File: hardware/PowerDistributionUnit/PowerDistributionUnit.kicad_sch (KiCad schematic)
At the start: 28 parts, among them J0 Conn_01x02, J1 Conn_01x02, J10 Conn_01x02, J11 Conn_01x02, J12 Conn_01x02, J13 Conn_01x02, J14 Conn_01x04, J15 Conn_01x04, J16 Conn_01x02, J2 Conn_01x02, J3 Conn_01x02, J4 Conn_01x02, J5 Conn_01x02, J6 Conn_01x02, J7 Conn_01x02, J8 Conn_01x02, J9 Conn_01x02

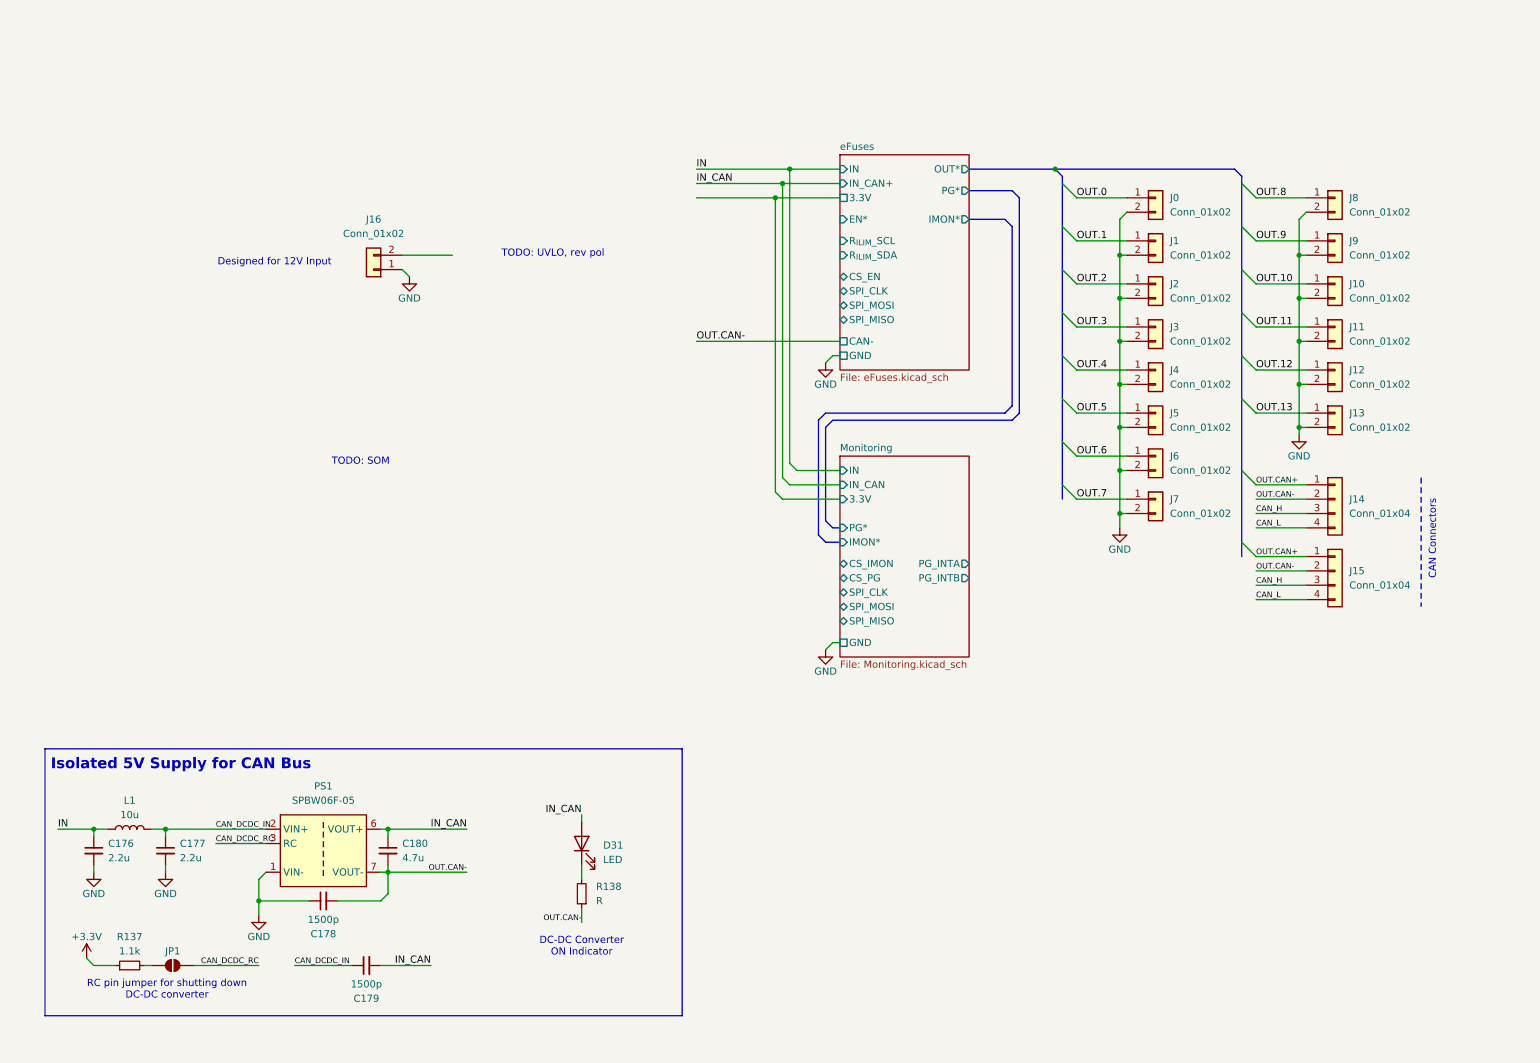
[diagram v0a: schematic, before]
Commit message: Added PSOM
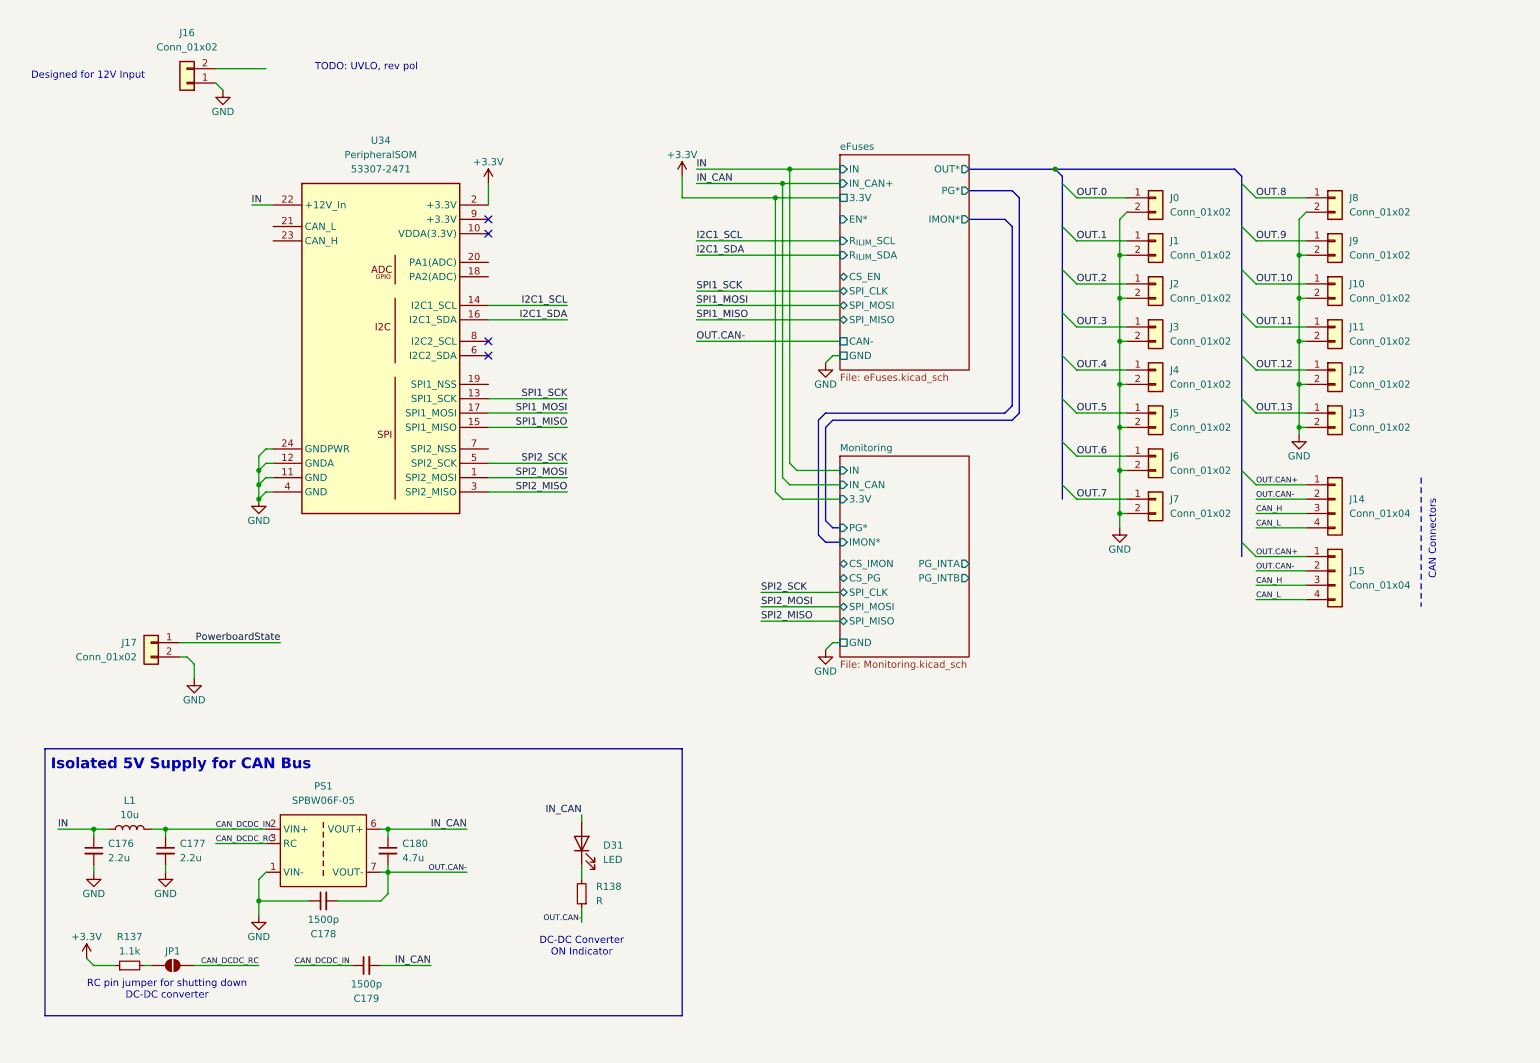
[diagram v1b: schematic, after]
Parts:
- added J17: Conn_01x02, symbol Connector_Generic:Conn_01x02
- added U34: PeripheralSOM, UTSVT_Special:PeripheralSOM, symbol utsvt-misc:PeripheralSOM
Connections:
- net +3.3V: now also U34.2 (+3.3V)
- net GND: now also J17.2 (Pin_2), U34.11 (GND), U34.12 (GNDA), U34.24 (GNDPWR), U34.4 (GND)
- net IN: now also U34.22 (+12V_In)
- new net I2C1_SCL: U34.14 (I2C1_SCL)
- new net I2C1_SDA: U34.16 (I2C1_SDA)
- new net PowerboardState: J17.1 (Pin_1)
- new net SPI1_MISO: U34.15 (SPI1_MISO)
- new net SPI1_MOSI: U34.17 (SPI1_MOSI)
- new net SPI1_SCK: U34.13 (SPI1_SCK)
- new net SPI2_MISO: U34.3 (SPI2_MISO)
- new net SPI2_MOSI: U34.1 (SPI2_MOSI)
- new net SPI2_SCK: U34.5 (SPI2_SCK)
- no-connect marks 0 -> 4
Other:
- note removed: "TODO: SOM"
- moved on the sheet: J16

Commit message: Added footprints, added pull-up resistors, finished wiring up SOM
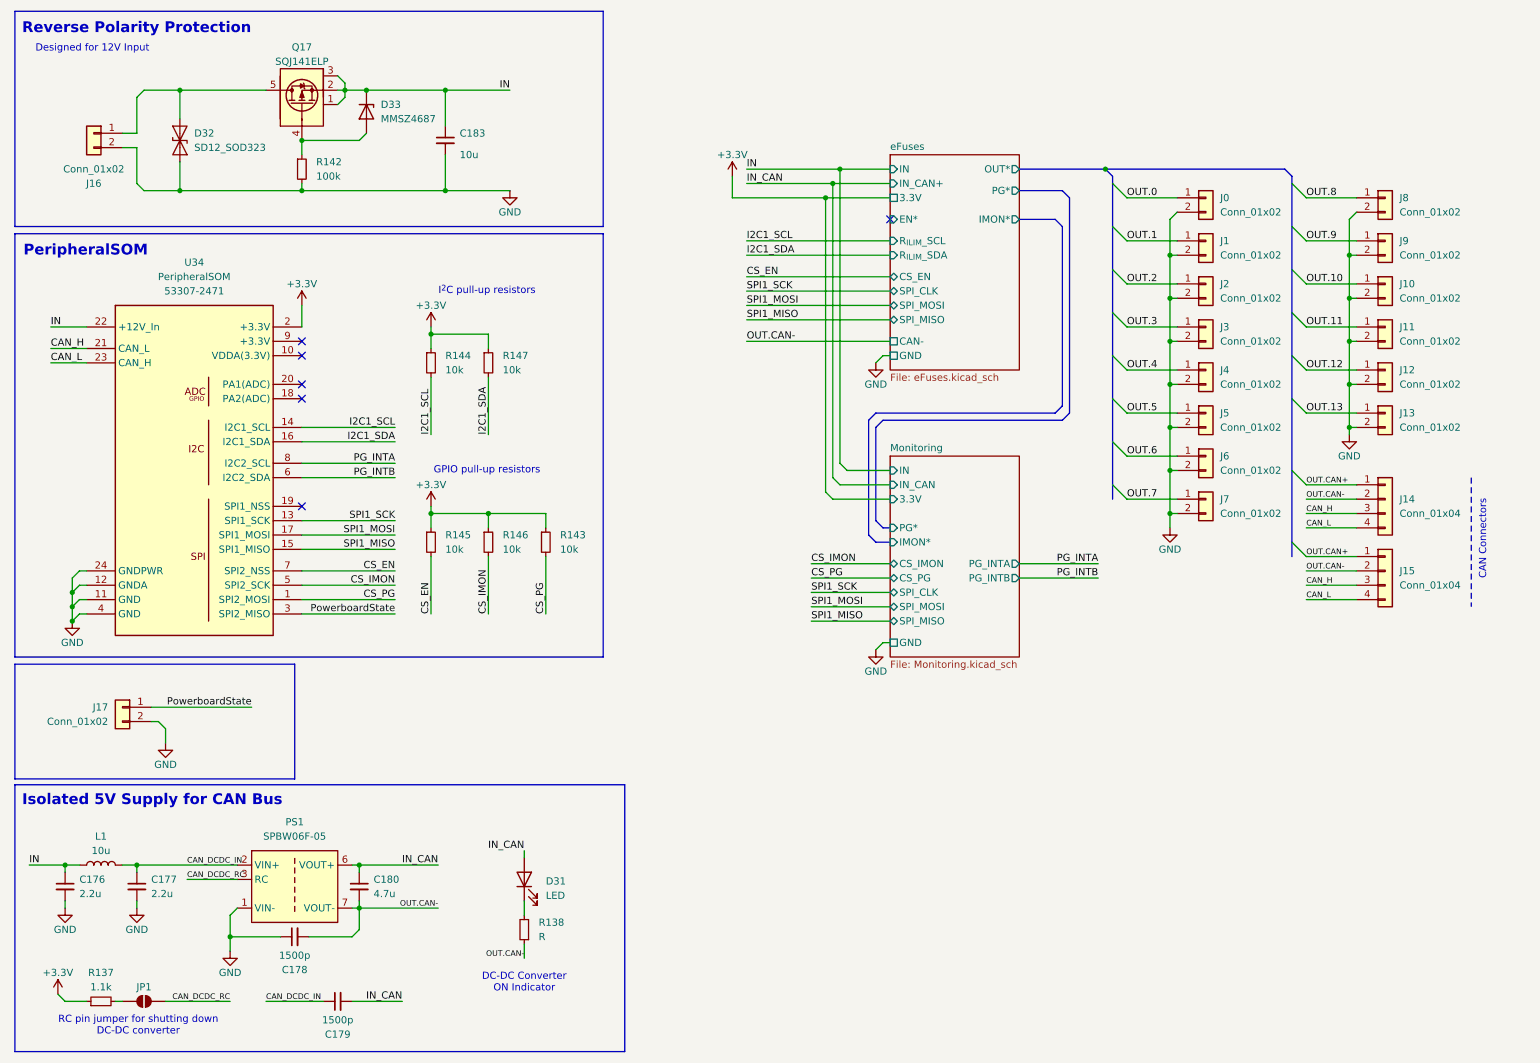
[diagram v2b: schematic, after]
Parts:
- added C183: 10u, symbol Device:C_Small
- added D32: SD12_SOD323, Diode_SMD:D_SOD-323, symbol Diode:SD12_SOD323
- added D33: MMSZ4687, Diode_SMD:D_SOD-123, symbol Device:D_Zener
- added Q17: SQJ141ELP, Package_SO:PowerPAK_SO-8L_Single, symbol PowerDistributionUnitLib:SQJ141ELP
- added R142: 100k, symbol Device:R_Small
- added R143, R144, R145, R146, R147: 10k, symbol Device:R_Small
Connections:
- net SPI2_MISO is gone; now on net PowerboardState: U34.3 (SPI2_MISO)
- net +3.3V: now also R143.1, R144.1, R145.1, R146.1, R147.1
- net CAN_H: now also U34.21 (CAN_L)
- net CAN_L: now also U34.23 (CAN_H)
- net GND: now also J16.2 (Pin_2), C183.2, D32.1 (A1), R142.2; no longer J16.1 (Pin_1)
- net I2C1_SCL: now also R144.2
- net I2C1_SDA: now also R147.2
- net IN: now also C183.1, D33.1 (K), Q17.1, Q17.2, Q17.3
- net PG_INTB: now reaches U34.6 (I2C2_SDA)
- net CS_EN: now reaches U34.7 (SPI2_NSS)
- net CS_EN: now also R145.2
- net PG_INTA: now reaches U34.8 (I2C2_SCL)
- net SPI2_MOSI renamed CS_PG
- net CS_PG: now also R143.2
- net SPI2_SCK renamed CS_IMON
- net CS_IMON: now also R146.2
- new net: D32.2 (A2), J16.1 (Pin_1), Q17.5
- new net: D33.2 (A), Q17.4, R142.1
- no-connect marks 4 -> 6
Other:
- note added: "GPIO pull-up resistors"
- note added: "I^{2}C pull-up resistors"
- note added: "PeripheralSOM"
- note added: "Reverse Polarity Protection"
- note removed: "TODO: UVLO, rev pol"
- moved on the sheet: C176, C177, C178, C179, C180, D31, J0, J1, J10, J11, J12, J13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

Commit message: Added non populated 0 ohm resistor
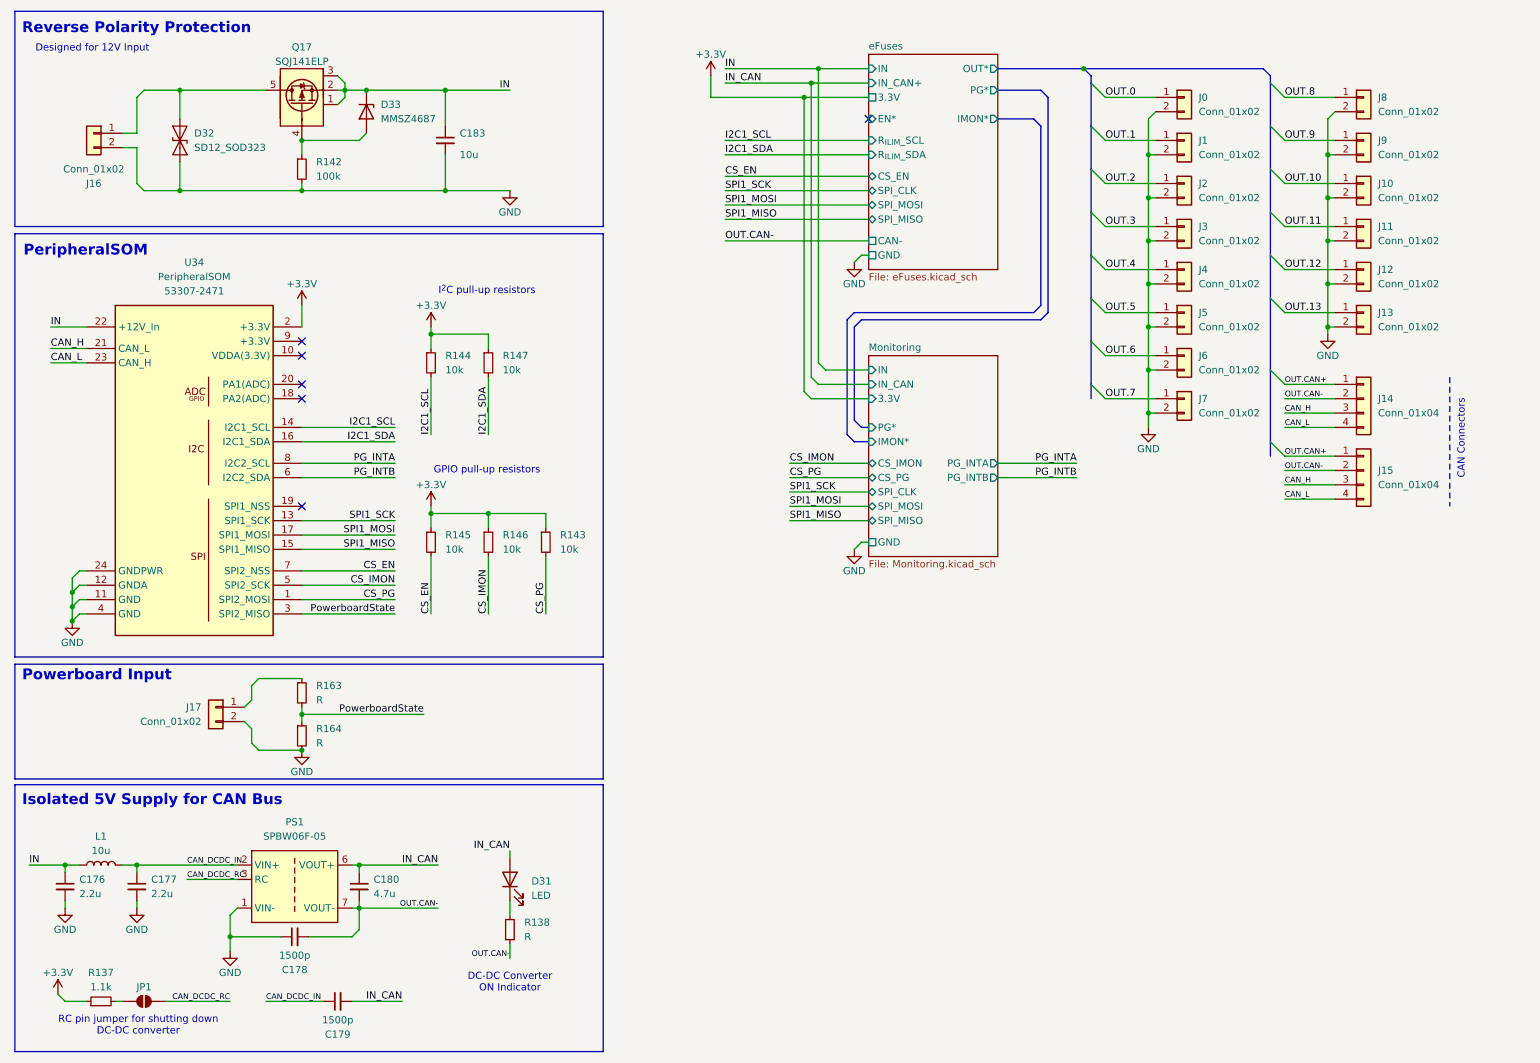
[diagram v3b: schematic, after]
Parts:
- added R163, R164: R, symbol Device:R_Small
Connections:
- net GND: now also R164.2
- net PowerboardState: now also R163.2, R164.1; no longer J17.1 (Pin_1)
- new net: J17.1 (Pin_1), R163.1
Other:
- note added: "Powerboard Input"
- moved on the sheet: D31, J0, J1, J10, J11, J12, J13, J14, J15, J17, J2, J3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
